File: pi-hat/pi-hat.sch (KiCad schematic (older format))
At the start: 67 parts, among them J1 Conn_01x04_Male, J2 Conn_01x04_Male, J3 Conn_01x05_Male, J4 Conn_01x05_Male, J5 Conn_01x05_Male, J6 Conn_01x05_Male, J7 Conn_01x07_Male, J8 Conn_01x07_Male, P1 Conn_02x20_Odd_Even, Q1 BSS138, Q10 AO 3415A, Q11 AO 3415A, Q12 BSS138, Q13 BSS138, Q14 BSS138, Q15 BSS138, Q16 BSS138, Q2 BSS138, Q3 BSS138, Q4 BC 807-25, Q5 AO 3415A, Q6 BC 807-25, Q7 BC 818-25, Q8 BC 818-25, Q9 BC 818-25, U1 M24C02-WMN

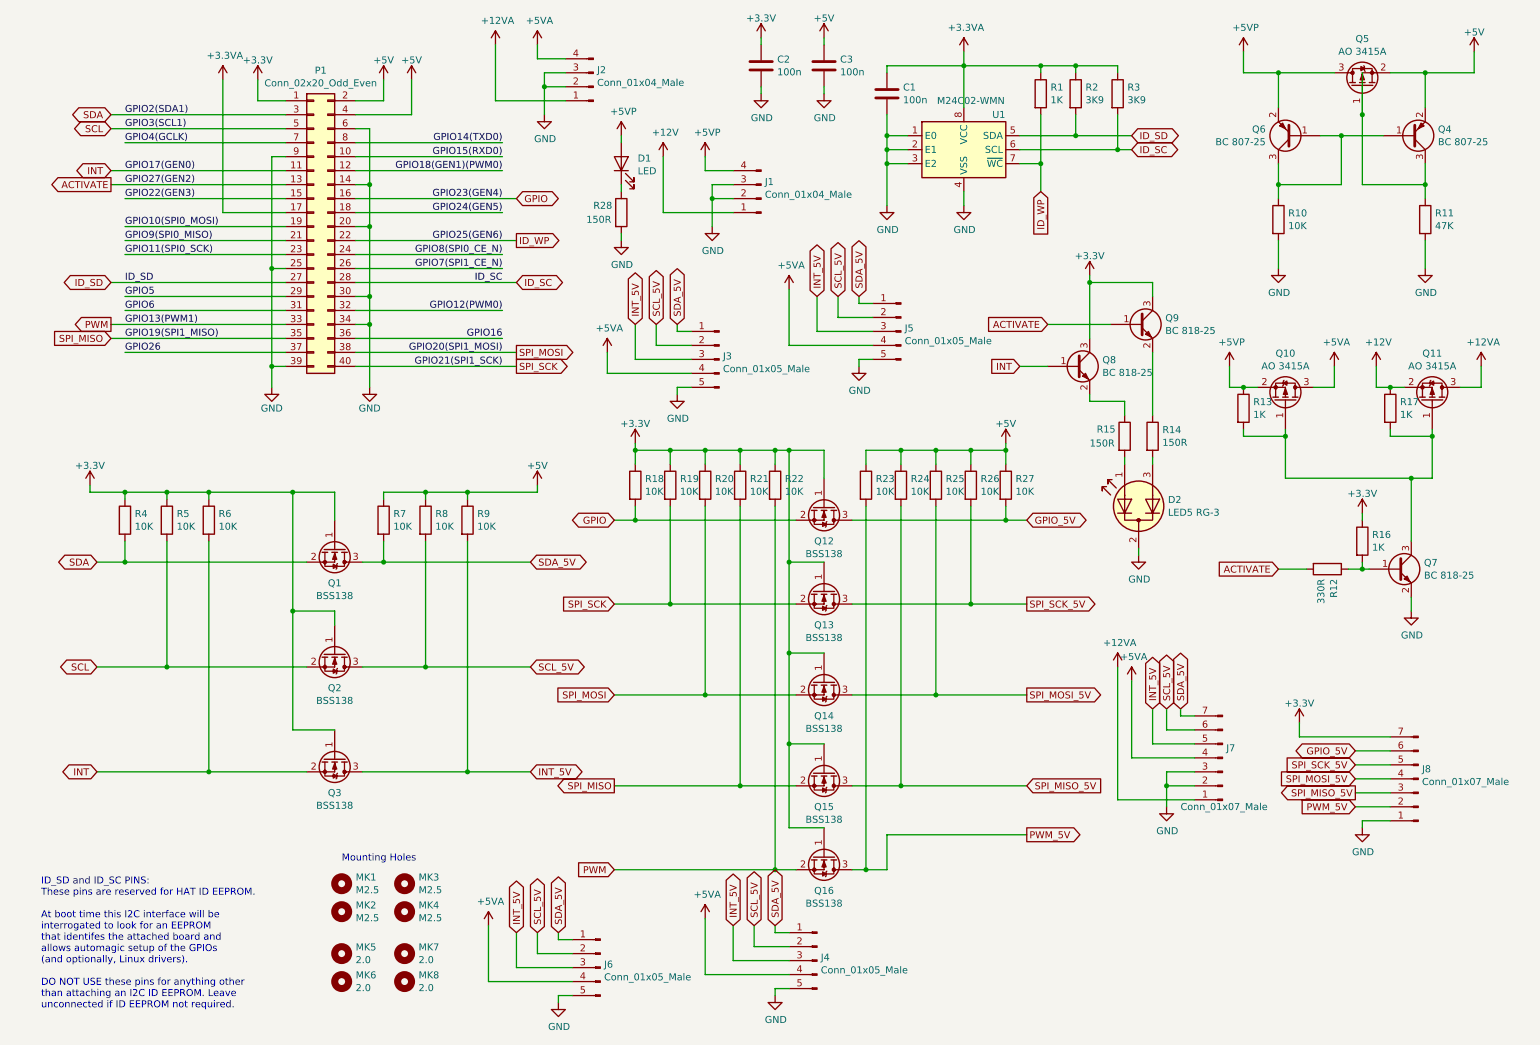
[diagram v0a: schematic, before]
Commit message: PiHat: 2nd revision
* Checked and adapted MOSFET high-side switches
* remove J6 for space and fix mounting hole
* Fix Molex connectors
* Capacitors
* Extension board positions
* General layout
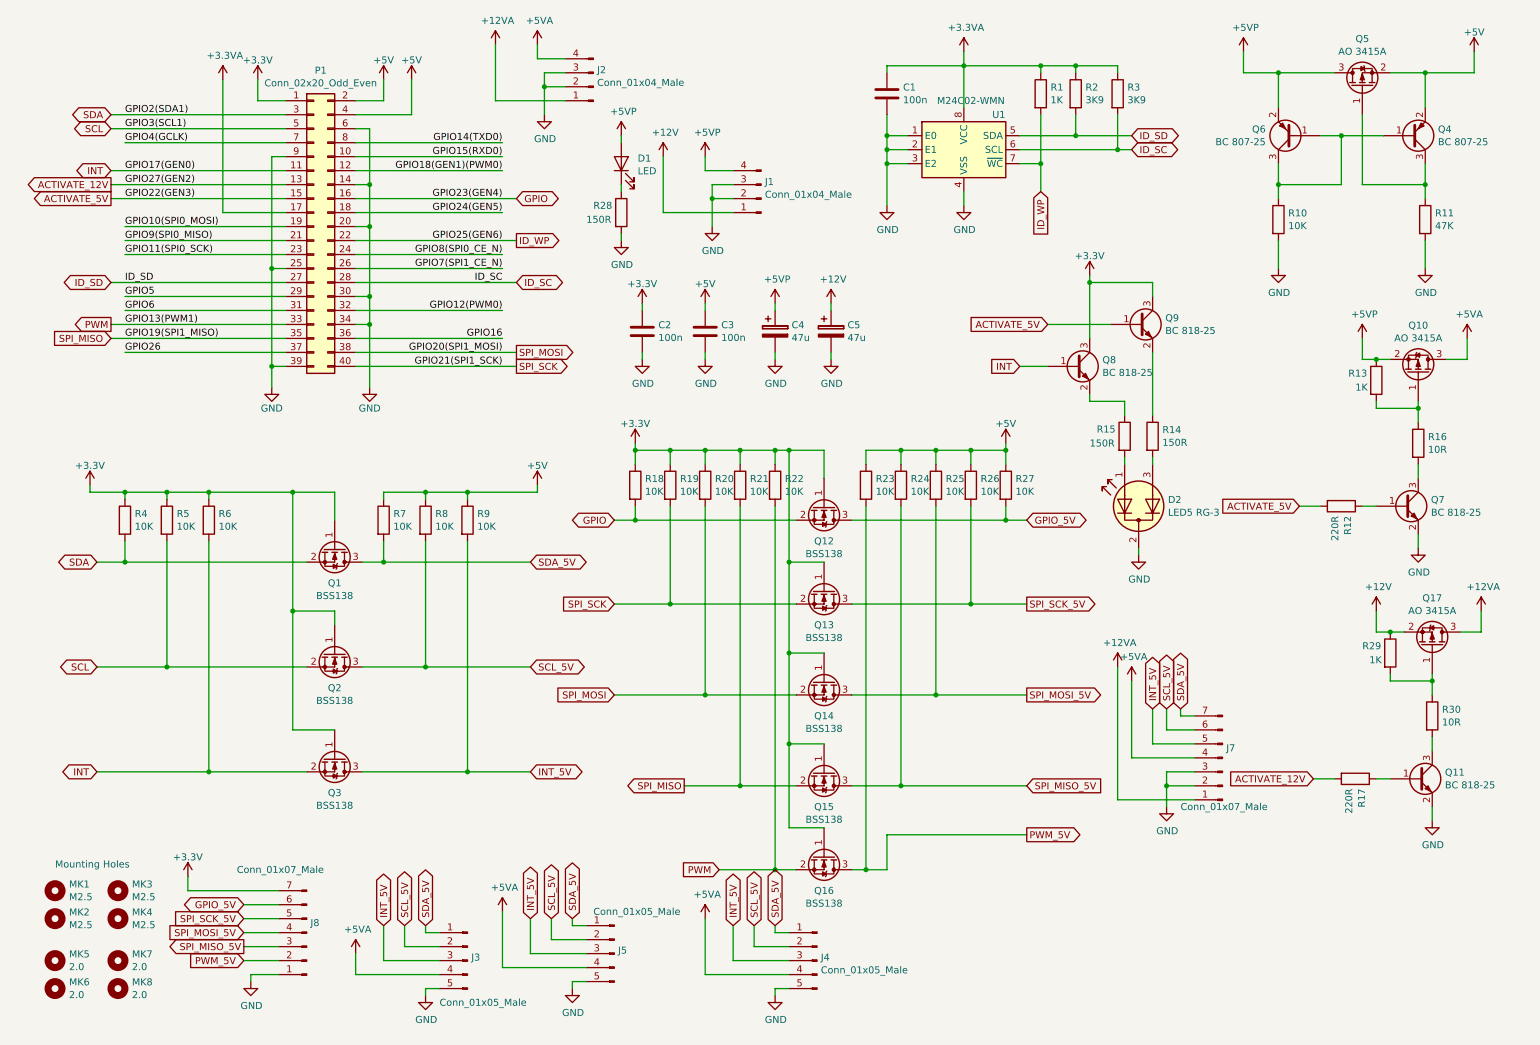
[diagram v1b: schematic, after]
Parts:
- removed J6: Conn_01x05_Male, Connector_PinHeader_2.54mm:PinHeader_1x05_P2.54mm_Vertical, symbol Connector:Conn_01x05_Male
- removed Q11: AO 3415A, Package_TO_SOT_SMD:SOT-23, symbol Device:Q_PMOS_GSD
- added C4, C5: 47u, Capacitor_SMD:CP_Elec_4x4.5, symbol Device:CP
- added Q11: BC 818-25, Package_TO_SOT_SMD:SOT-23, symbol Device:Q_NPN_BEC
- added Q17: AO 3415A, Package_TO_SOT_SMD:SOT-23, symbol Device:Q_PMOS_GSD
- added R29: 1K, Capacitor_SMD:C_0603_1608Metric_Pad1.05x0.95mm_HandSolder, symbol Device:R
- added R30: 10R, Capacitor_SMD:C_0603_1608Metric_Pad1.05x0.95mm_HandSolder, symbol Device:R
- R12: value 330R -> 220R
- R16: value 1K -> 10R
- R17: value 1K -> 220R
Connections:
- net GPIO22(GEN3) is gone; now on net ACTIVATE_5V: P1.15 (Pin_15)
- net +12V: now also C5.1, Q17.2 (S), R29.1; no longer R17.1
- net +12VA: now also Q17.3 (D)
- net +3V3: no longer R16.1
- net +5VP: now also C4.1
- net GND: now also C4.2, C5.2, Q11.2 (E)
- net at Q7.1 (B), R12.1: no longer R16.2
- net at Q10.1 (G), R13.2: now also R16.1; no longer Q7.3 (C), R17.2
- net ACTIVATE renamed ACTIVATE_5V
- net ACTIVATE_5V: no longer P1.13 (Pin_13)
- new net: Q7.3 (C), R16.2
- new net: Q17.1 (G), R29.2, R30.1
- new net: Q11.3 (C), R30.2
- new net: Q11.1 (B), R17.1
- new net ACTIVATE_12V: P1.13 (Pin_13), R17.2
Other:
- note removed: "ID_SD and ID_SC PINS:\nThese pins are reserved for HAT ID EEPROM.\n\nAt boot time this I2C interface will be\ninterrogated to look for an EEPROM\nthat identifes the attached board and\nallows automagic setup of the GPIOs\n(and optionally, Linux drivers).\n\nDO NOT USE these pins for anything other\nthan attaching an I2C ID EEPROM. Leave\nunconnected if ID EEPROM not required."
- moved on the sheet: C2, C3, J3, J5, J8, MK1, MK2, MK3, MK4, MK5, MK6, MK7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

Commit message: Final fixes
* make sheet bigger (A3) to fix everything nicely
* fix INT LED to be low active
* fix molex holes
* fix base resistors
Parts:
- added R31, R32: 330R, Capacitor_SMD:C_0603_1608Metric_Pad1.05x0.95mm_HandSolder, symbol Device:R
- R12, R17: value 220R -> 330R
- R13, R29: value 1K -> 100K
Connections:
- net +3V3: now also R15.1; no longer Q8.3 (C)
- net ACTIVATE_5V: now also R32.1; no longer Q9.1 (B)
- net GND: now also Q8.2 (E)
- net INT: now also R31.2; no longer Q8.1 (B)
- net at D2.1 (A1), R15.2: now also Q8.3 (C)
- new net: Q8.1 (B), R31.1
- new net: Q9.1 (B), R32.2
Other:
- moved on the sheet: C1, C2, C3, C4, C5, D1, D2, J1, J2, J3, J4, J5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

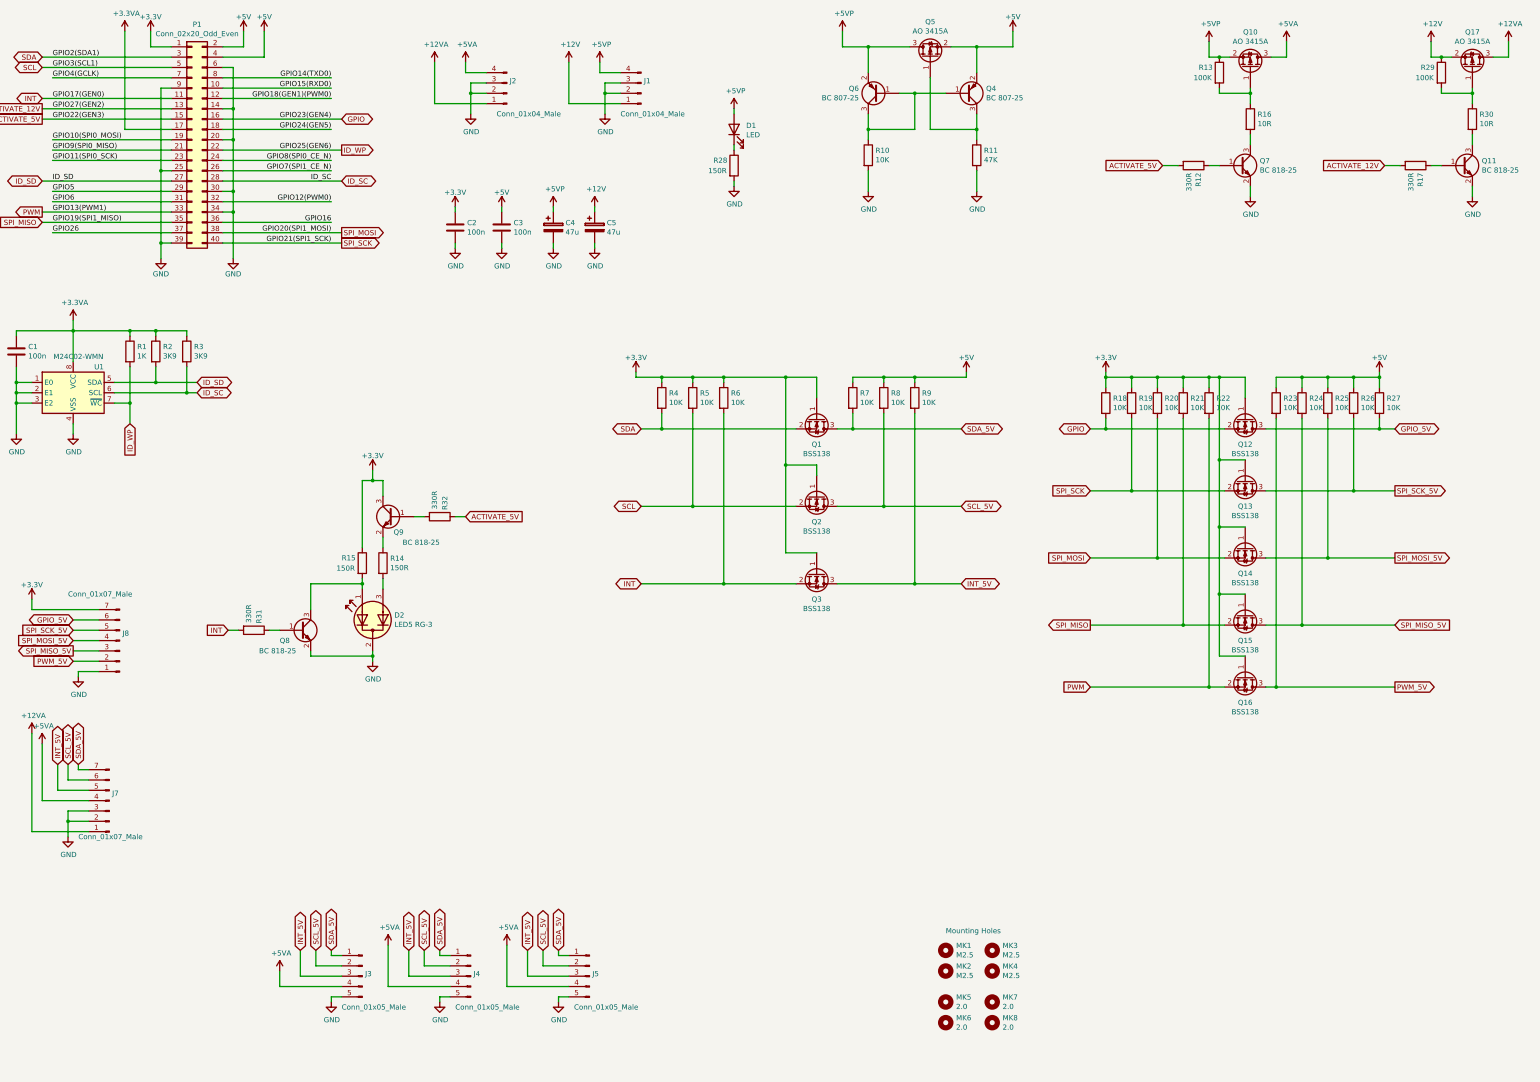
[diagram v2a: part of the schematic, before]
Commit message: Add matching resistors to I3C lines
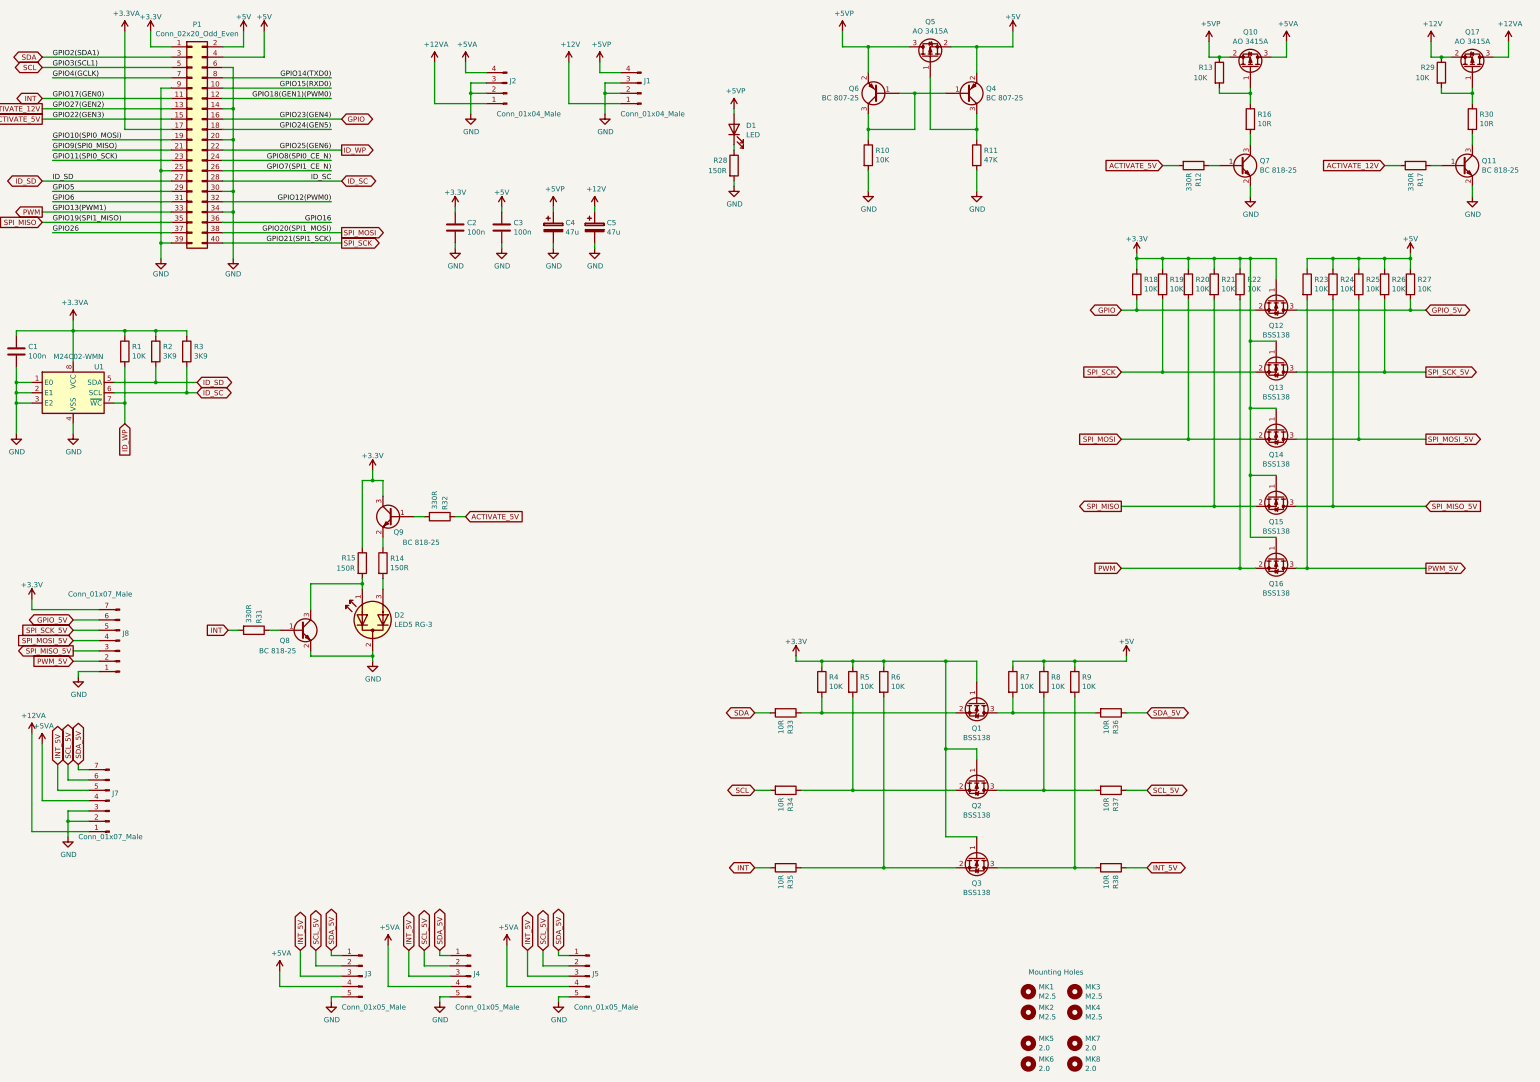
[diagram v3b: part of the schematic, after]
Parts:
- added R33, R34, R35, R36, R37, R38: 10R, Capacitor_SMD:C_0603_1608Metric_Pad1.05x0.95mm_HandSolder, symbol Device:R
- R1: value 1K -> 10K
- R13, R29: value 100K -> 10K
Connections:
- net INT: now also R35.2; no longer Q3.2 (S), R6.2
- net INT_5V: now also R38.1; no longer Q3.3 (D), R9.2
- net SCL: now also R34.2; no longer Q2.2 (S), R5.2
- net SCL_5V: now also R37.1; no longer Q2.3 (D), R8.2
- net SDA: now also R33.2; no longer Q1.2 (S), R4.2
- net SDA_5V: now also R36.1; no longer Q1.3 (D), R7.2
- new net: Q2.2 (S), R34.1, R5.2
- new net: Q2.3 (D), R37.2, R8.2
- new net: Q1.2 (S), R33.1, R4.2
- new net: Q1.3 (D), R36.2, R7.2
- new net: Q3.2 (S), R35.1, R6.2
- new net: Q3.3 (D), R38.2, R9.2
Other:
- moved on the sheet: MK1, MK2, MK3, MK4, MK5, MK6, MK7, MK8, Q1, Q12, Q13, Q14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
